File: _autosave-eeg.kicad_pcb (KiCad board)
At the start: 2 copper layers, 75.7 x 54.9 mm, 128 parts, among them J1 USB_B_Mini, J2 Conn_01x10_MountingPin, U1 STM32F446RE, U10 -.+2.5V.+3.3V-GND, U11 +5V, U12 RN4678-V_RM100, U2 ADS1299-8CHANNEL, U3 LD39050PU33R, U4 TPS60403DBVT, U5 TPS73225DBVT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

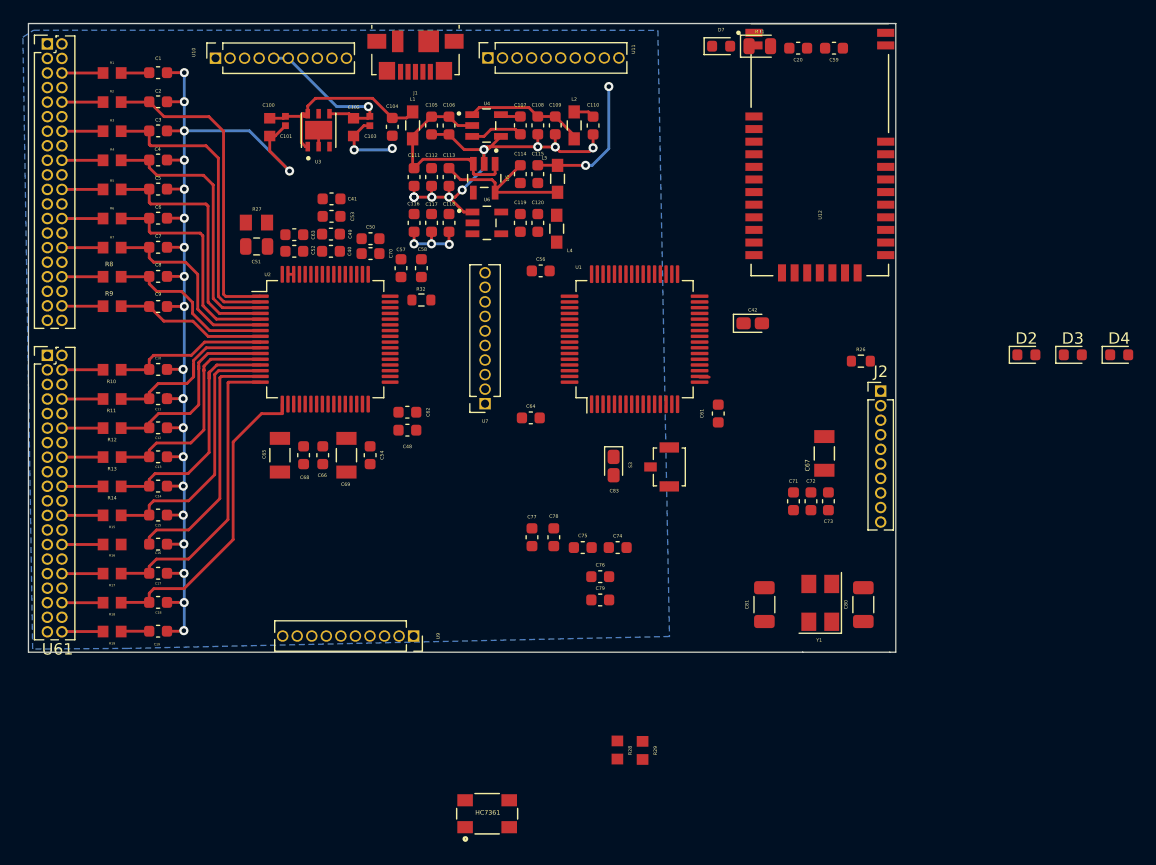
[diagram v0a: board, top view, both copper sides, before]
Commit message: AVDD and AVSS capacitors are placed
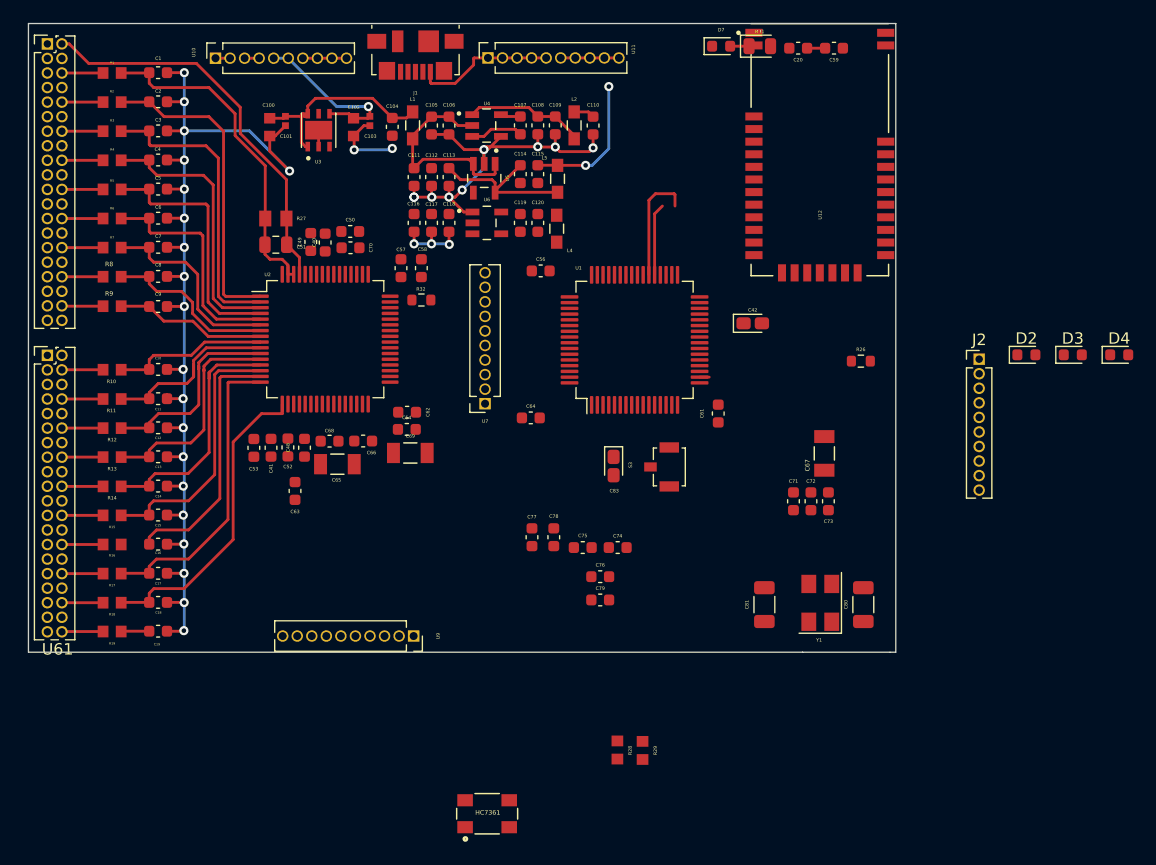
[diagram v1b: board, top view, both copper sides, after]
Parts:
- moved C63 22.4 mm to (61.4, 70.8), turned to 270 degrees
- moved C41 22.3 mm to (59.3, 67.0), turned to 270 degrees
- moved C53 21.3 mm to (57.8, 67.0), turned to 270 degrees
- moved C52 17.1 mm to (60.7, 67.0), turned to 90 degrees
- moved C48 9.11 mm to (62.2, 67.0), turned to 90 degrees
- moved J2 9.03 mm to (121.1, 59.3)
- moved C69 5.58 mm to (71.4, 67.4), turned to 0 degrees
- moved C65 5.08 mm to (65.1, 68.4), turned to 0 degrees
- moved C54 3.92 mm to (71.1, 65.4), turned to 0 degrees
- moved C66 3.74 mm to (67.3, 66.4), turned to 0 degrees
- moved C68 2.57 mm to (64.4, 66.4), turned to 180 degrees
- moved C49 1.89 mm to (62.7, 49.0), turned to 90 degrees
- moved C50 1.88 mm to (66.2, 48.1)
- moved C70 1.82 mm to (66.2, 49.5)
- moved R27 1.73 mm to (59.7, 47.0)
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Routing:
- net /BIASINV: track 0.00 -> 34.6 mm
- net /BIASIN: track 2.96 -> 29.0 mm
- net +5V: track 18.2 -> 30.5 mm
- net /USART6_RX: track 0.00 -> 10.1 mm
- net GND: track 0.00 -> 8.89 mm
- net /USART6_TX: track 0.00 -> 6.29 mm
- net Net-(D7-Pad2): track 0.00 -> 1.65 mm
- net +3V3: track 14.7 -> 16.2 mm
- net +2V5: track 12.2 -> 13.5 mm
- net -2V5: track 0.04 -> 1.27 mm
- removed copper zone on B.Cu, net GNDA
